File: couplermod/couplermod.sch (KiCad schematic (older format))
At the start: 6 parts, among them J1 SMA, P1 CONN_2

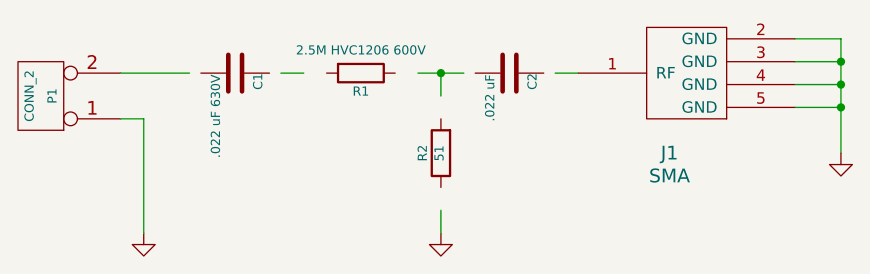
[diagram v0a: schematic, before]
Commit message: added bc637 pcie dsub15 clock/pps breakout
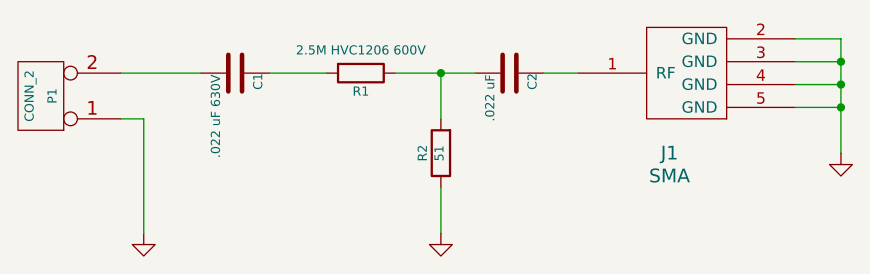
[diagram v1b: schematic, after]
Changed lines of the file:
@@
 LIBS:memory
 LIBS:xilinx
-LIBS:special
 LIBS:microcontrollers
 LIBS:dsp
@@
 LIBS:sma
 LIBS:couplermod-cache
-EELAYER 24 0
+EELAYER 25 0
 EELAYER END
 $Descr A4 11693 8268
@@
 $EndComp
 Wire Wire Line
-	6100 3200 6200 3200
+	6050 3200 6200 3200
 $Comp
 L R R1
@@
 $EndComp
 Wire Wire Line
-	5500 3200 5700 3200
+	5400 3200 5750 3200
 Wire Wire Line
-	5600 3300 5600 3200
+	5600 3200 5600 3400
 Connection ~ 5600 3200
 $Comp
@@
 $EndComp
 Wire Wire Line
-	5600 3900 5600 3800
+	5600 3700 5600 3900
 Wire Wire Line
-	4900 3200 5000 3200
+	4850 3200 5100 3200
 $Comp
 L CONN_2 P1
@@
 $EndComp
 Wire Wire Line
-	4200 3200 4500 3200
+	4200 3200 4550 3200
 $Comp
 L GND #PWR1
